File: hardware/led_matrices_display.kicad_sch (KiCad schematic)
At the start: 5 parts, among them J2 SS-108-TT-2, U10 KWM-20882CUYB, U11 KWM-20882CUYB, U12 KWM-20882CUYB, U13 KWM-20882CUYB

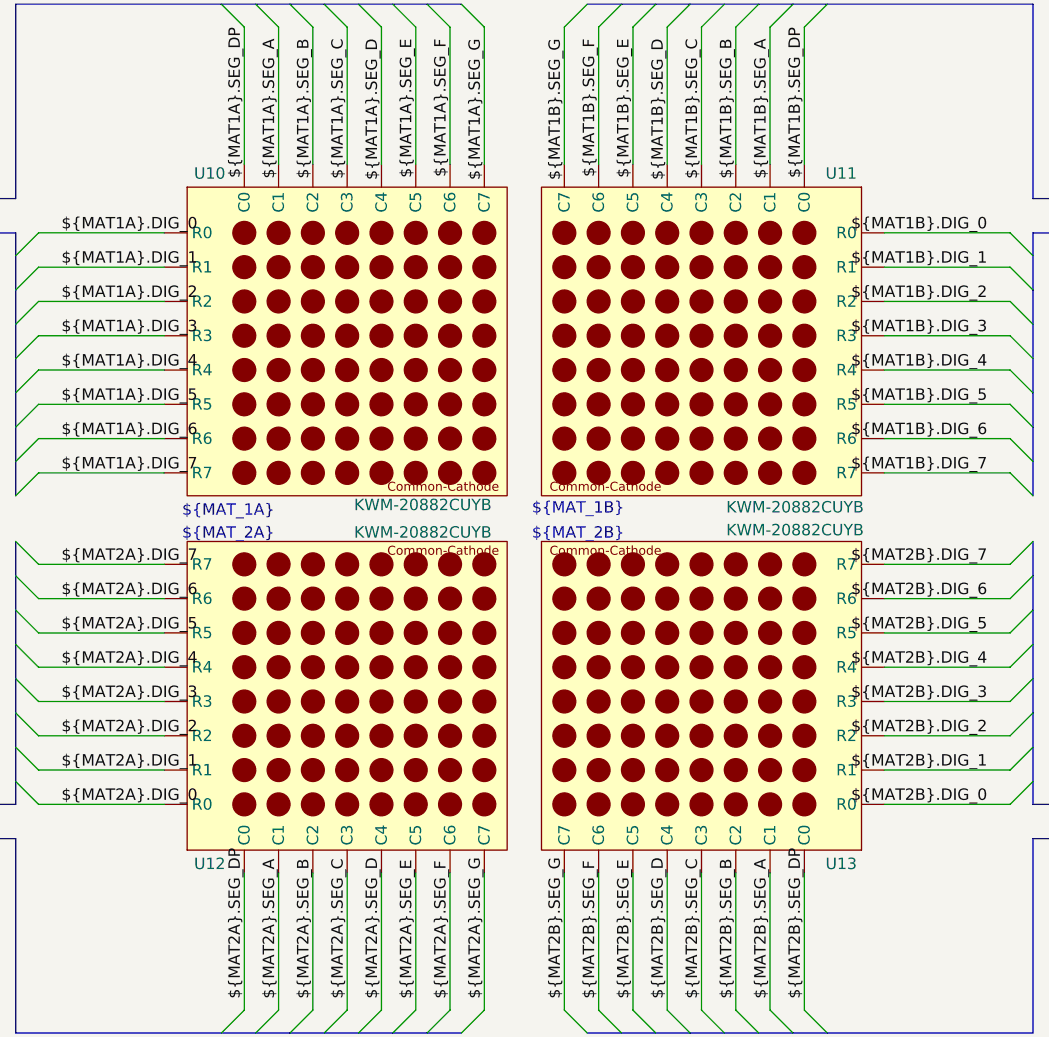
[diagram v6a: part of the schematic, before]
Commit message: Removed comments on UART, added some footprints and started fixing rule checks
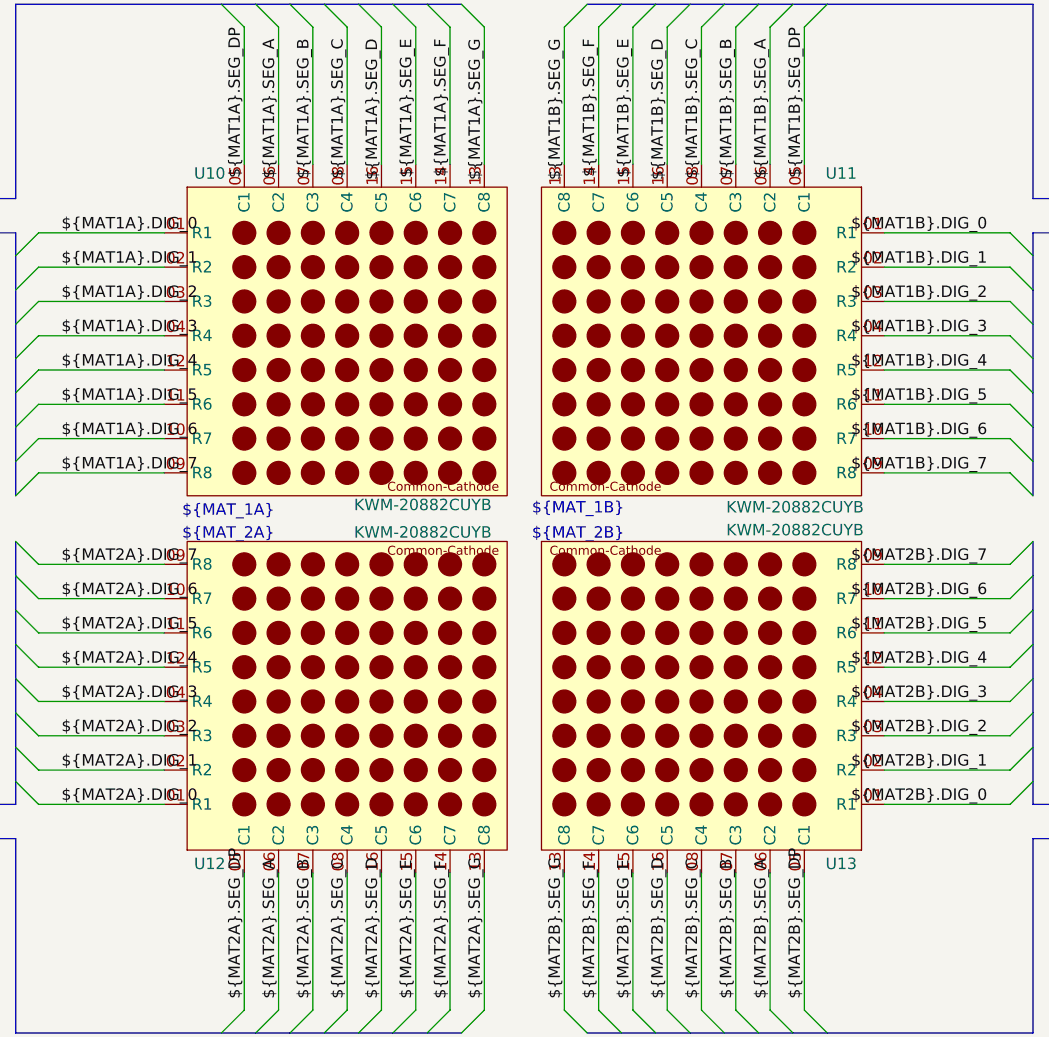
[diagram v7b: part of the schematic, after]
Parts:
- J2: MANUFACTURER Samtec Inc. -> (none); Manuf. Name (none) -> Samtec Inc.; Manuf. Part # (none) -> SS-108-TT-2; PARTREV R -> (none); Part Num SS-108-TT-2 -> (none); Price/unit 11,73 kr -> (none); STANDARD Manufacturer Recommendations -> (none); Supplier Name (none) -> MOUSER; Supplier Unit Price (none) -> 11,73 kr
- U10, U11, U12, U13: footprint (none) -> Project-kitchen_timer:KWM-20882CUYB; Manuf. Part # (none) -> KWM-2088CUYB; Part Num KWM-2088CUYB -> (none); Price/unit 75,00 kr -> (none); Supplier Name (none) -> ELECTROKIT; Supplier Unit Price (none) -> 75,00 kr
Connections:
- net ${MAT1A}.DIG_0: now also U10.01 (R1); no longer U10. (C7)
- net ${MAT1A}.DIG_1: now also U10.02 (R2); no longer U10. (C7)
- net ${MAT1A}.DIG_2: now also U10.03 (R3); no longer U10. (C7)
- net ${MAT1A}.DIG_3: now also U10.04 (R4); no longer U10. (C7)
- net ${MAT1A}.DIG_4: now also U10.12 (R5); no longer U10. (C7)
- net ${MAT1A}.DIG_5: now also U10.11 (R6); no longer U10. (C7)
- net ${MAT1A}.DIG_6: now also U10.10 (R7); no longer U10. (C7)
- net ${MAT1A}.DIG_7: now also U10.09 (R8); no longer U10. (C7)
- net ${MAT1A}.SEG_A: now also U10.06 (C2); no longer U10. (C7)
- net ${MAT1A}.SEG_B: now also U10.07 (C3); no longer U10. (C7)
- net ${MAT1A}.SEG_C: now also U10.08 (C4); no longer U10. (C7)
- net ${MAT1A}.SEG_D: now also U10.16 (C5); no longer U10. (C7)
- net ${MAT1A}.SEG_DP: now also U10.05 (C1); no longer U10. (C7)
- net ${MAT1A}.SEG_E: now also U10.15 (C6); no longer U10. (C7)
- net ${MAT1A}.SEG_F: now also U10.14 (C7); no longer U10. (C7)
- net ${MAT1A}.SEG_G: now also U10.13 (C8); no longer U10. (C7)
- net ${MAT1B}.DIG_0: now also U11.01 (R1); no longer U11. (C7)
- net ${MAT1B}.DIG_1: now also U11.02 (R2); no longer U11. (C7)
- net ${MAT1B}.DIG_2: now also U11.03 (R3); no longer U11. (C7)
- net ${MAT1B}.DIG_3: now also U11.04 (R4); no longer U11. (C7)
- net ${MAT1B}.DIG_4: now also U11.12 (R5); no longer U11. (C7)
- net ${MAT1B}.DIG_5: now also U11.11 (R6); no longer U11. (C7)
- net ${MAT1B}.DIG_6: now also U11.10 (R7); no longer U11. (C7)
- net ${MAT1B}.DIG_7: now also U11.09 (R8); no longer U11. (C7)
- net ${MAT1B}.SEG_A: now also U11.06 (C2); no longer U11. (C7)
- net ${MAT1B}.SEG_B: now also U11.07 (C3); no longer U11. (C7)
- net ${MAT1B}.SEG_C: now also U11.08 (C4); no longer U11. (C7)
- net ${MAT1B}.SEG_D: now also U11.16 (C5); no longer U11. (C7)
- net ${MAT1B}.SEG_DP: now also U11.05 (C1); no longer U11. (C7)
- net ${MAT1B}.SEG_E: now also U11.15 (C6); no longer U11. (C7)
- net ${MAT1B}.SEG_F: now also U11.14 (C7); no longer U11. (C7)
- net ${MAT1B}.SEG_G: now also U11.13 (C8); no longer U11. (C7)
- net ${MAT2A}.DIG_0: now also U12.01 (R1); no longer U12. (C7)
- net ${MAT2A}.DIG_1: now also U12.02 (R2); no longer U12. (C7)
- net ${MAT2A}.DIG_2: now also U12.03 (R3); no longer U12. (C7)
- net ${MAT2A}.DIG_3: now also U12.04 (R4); no longer U12. (C7)
- net ${MAT2A}.DIG_4: now also U12.12 (R5); no longer U12. (C7)
- net ${MAT2A}.DIG_5: now also U12.11 (R6); no longer U12. (C7)
- net ${MAT2A}.DIG_6: now also U12.10 (R7); no longer U12. (C7)
- net ${MAT2A}.DIG_7: now also U12.09 (R8); no longer U12. (C7)
- net ${MAT2A}.SEG_A: now also U12.06 (C2); no longer U12. (C7)
- net ${MAT2A}.SEG_B: now also U12.07 (C3); no longer U12. (C7)
- net ${MAT2A}.SEG_C: now also U12.08 (C4); no longer U12. (C7)
- net ${MAT2A}.SEG_D: now also U12.16 (C5); no longer U12. (C7)
- net ${MAT2A}.SEG_DP: now also U12.05 (C1); no longer U12. (C7)
- net ${MAT2A}.SEG_E: now also U12.15 (C6); no longer U12. (C7)
- net ${MAT2A}.SEG_F: now also U12.14 (C7); no longer U12. (C7)
- net ${MAT2A}.SEG_G: now also U12.13 (C8); no longer U12. (C7)
- net ${MAT2B}.DIG_0: now also U13.01 (R1); no longer U13. (C7)
- net ${MAT2B}.DIG_1: now also U13.02 (R2); no longer U13. (C7)
- net ${MAT2B}.DIG_2: now also U13.03 (R3); no longer U13. (C7)
- net ${MAT2B}.DIG_3: now also U13.04 (R4); no longer U13. (C7)
- net ${MAT2B}.DIG_4: now also U13.12 (R5); no longer U13. (C7)
- net ${MAT2B}.DIG_5: now also U13.11 (R6); no longer U13. (C7)
- net ${MAT2B}.DIG_6: now also U13.10 (R7); no longer U13. (C7)
- net ${MAT2B}.DIG_7: now also U13.09 (R8); no longer U13. (C7)
- net ${MAT2B}.SEG_A: now also U13.06 (C2); no longer U13. (C7)
- net ${MAT2B}.SEG_B: now also U13.07 (C3); no longer U13. (C7)
- net ${MAT2B}.SEG_C: now also U13.08 (C4); no longer U13. (C7)
- net ${MAT2B}.SEG_D: now also U13.16 (C5); no longer U13. (C7)
- net ${MAT2B}.SEG_DP: now also U13.05 (C1); no longer U13. (C7)
- net ${MAT2B}.SEG_E: now also U13.15 (C6); no longer U13. (C7)
- net ${MAT2B}.SEG_F: now also U13.14 (C7); no longer U13. (C7)
- net ${MAT2B}.SEG_G: now also U13.13 (C8); no longer U13. (C7)

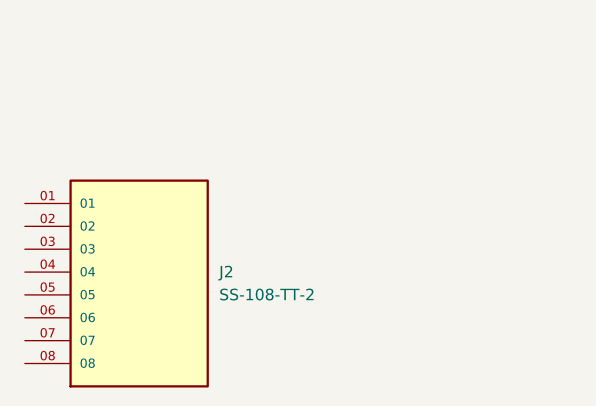
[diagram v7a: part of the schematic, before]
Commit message: Added many footprints and populated part of the property tables
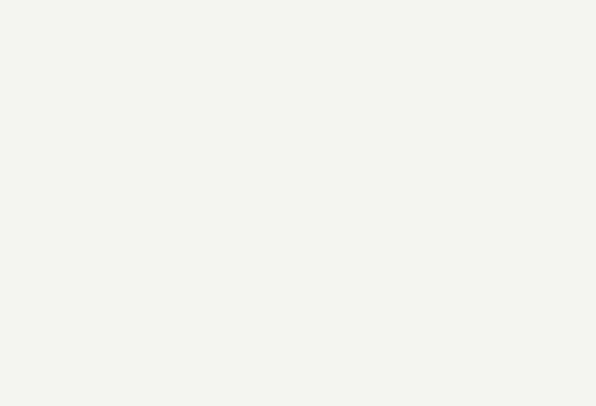
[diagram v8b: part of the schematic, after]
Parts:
- removed J2: SS-108-TT-2, kitchen_timer:SAMTEC_SS-108-TT-2, symbol kitchen_timer-symbols_lib:SS-108-TT-2
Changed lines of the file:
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@@
-		)
-	)
-	(symbol
-		(lib_id "kitchen_timer-symbols_lib:SS-108-TT-2")
-		(at 31.75 185.42 0)
-		(unit 1)
-		(exclude_from_sim no)
-		(in_bom yes)
-		(on_board yes)
-		(dnp no)
-		(fields_autoplaced yes)
-		(property "Reference" "J2"
-			(at 40.64 182.8799 0)
-			(effects
-				(font
-					(size 1.27 1.27)
-				)
-				(justify left)
-			)
-		)
-		(property "Value" "SS-108-TT-2"
-			(at 40.64 185.4199 0)
-			(effects
-				(font
-					(size 1.27 1.27)
-				)
-				(justify left)
-			)
-		)
-		(property "Footprint" "kitchen_timer:SAMTEC_SS-108-TT-2"
-			(at 31.75 185.42 0)
-			(effects
-				(font
-					(size 1.27 1.27)
-				)
-				(justify bottom)
-				(hide yes)
-			)
-		)
-		(property "Datasheet" "https://suddendocs.samtec.com/catalog_english/ss.pdf"
-			(at 31.75 185.42 0)
-			(effects
-				(font
-					(size 1.27 1.27)
-				)
-				(hide yes)
-			)
-		)
-		(property "Description" "Headers & Wire Housings .100\" Single Row Screw Machine Socket Strip"
-			(at 31.75 185.42 0)
-			(effects
-				(font
-					(size 1.27 1.27)
-				)
-				(hide yes)
-			)
-		)
-		(property "Supplier Link" "https://www.mouser.se/ProductDetail/Samtec/SS-108-TT-2?qs=rU5fayqh%252BE1eQOsz7NCRKg%3D%3D"
-			(at 31.75 185.42 0)
-			(effects
-				(font
-					(size 1.27 1.27)
-				)
-				(hide yes)
-			)
-		)
-		(property "Package" "Through Hole"
-			(at 31.75 185.42 0)
-			(effects
-				(font
-					(size 1.27 1.27)
-				)
-				(hide yes)
-			)
-		)
-		(property "Manuf. Name" "Samtec Inc."
-			(at 31.75 185.42 0)
-			(effects
-				(font
-					(size 1.27 1.27)
-				)
-				(hide yes)
-			)
-		)
-		(property "Supplier Name" "MOUSER"
-			(at 31.75 185.42 0)
-			(effects
-				(font
-					(size 1.27 1.27)
-				)
-				(hide yes)
-			)
-		)
-		(property "Manuf. Part #" "SS-108-TT-2"
-			(at 31.75 185.42 0)
-			(effects
-				(font
-					(size 1.27 1.27)
-				)
-				(hide yes)
-			)
-		)
-		(property "Supplier Unit Price" "11,73 kr"
-			(at 31.75 185.42 0)
-			(effects
-				(font
-					(size 1.27 1.27)
-				)
-				(hide yes)
-			)
-		)
-		(pin "05"
-		)
-		(pin "02"
-		)
-		(pin "03"
-		)
-		(pin "07"
-		)
-		(pin "08"
-		)
-		(pin "01"
-		)
-		(pin "04"
-		)
-		(pin "06"
-		)
-		(instances
-			(project ""
-				(path "/8963deea-96bc-4401-b671-98fbe9ed9c6a/51b07aee-e177-4be7-b84e-75e5e68b78bc"
-					(reference "J2")
-					(unit 1)
-				)
-			)
 		)
 	)
